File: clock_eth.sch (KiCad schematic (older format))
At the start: 4 parts, among them X2 ASE-xxxMHz

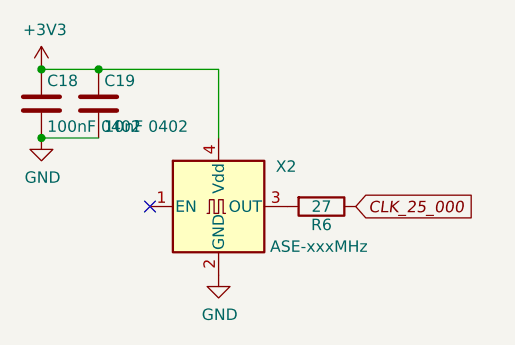
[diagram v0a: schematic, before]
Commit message: 27->33 ohms (basic...)
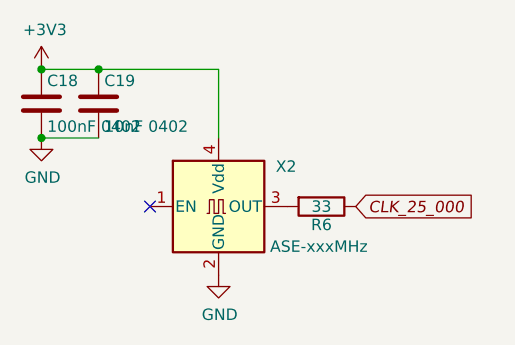
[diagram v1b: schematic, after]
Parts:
- R8: value 27 -> 33; MPN 0402WGF270JTCE -> 0402WGF330JTCE
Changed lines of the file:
@@
 AR Path="/6567C857/65008AD6" Ref="R6"  Part="1"
 F 0 "R6" V 4480 3050 50  0000 C CNN
-F 1 "27" V 4400 3050 50  0000 C CNN
+F 1 "33" V 4400 3050 50  0000 C CNN
 F 2 "Resistor_SMD:R_0402_1005Metric" V 4330 3050 50  0001 C CNN
 F 3 "" H 4400 3050 50  0000 C CNN
-F 4 "0402WGF270JTCE" V 4400 3050 50  0001 C CNN "MPN"
+F 4 "0402WGF330JTCE" V 4400 3050 50  0001 C CNN "MPN"
 F 5 "" V 4400 2450 50  0001 C CNN "MPN-ALT"
 F 6 "https://lcsc.com/product-detail/Chip-Resistor-Surface-Mount_UNI-ROYAL-Uniroyal-Elec-0603WAF270JT5E_C25190.html" V 4400 3050 50  0001 C CNN "URL"
